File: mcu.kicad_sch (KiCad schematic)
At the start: 16 parts, among them J1 Conn_ARM_SWD_TagConnect_TC2030, U2 STM32L053R8Tx

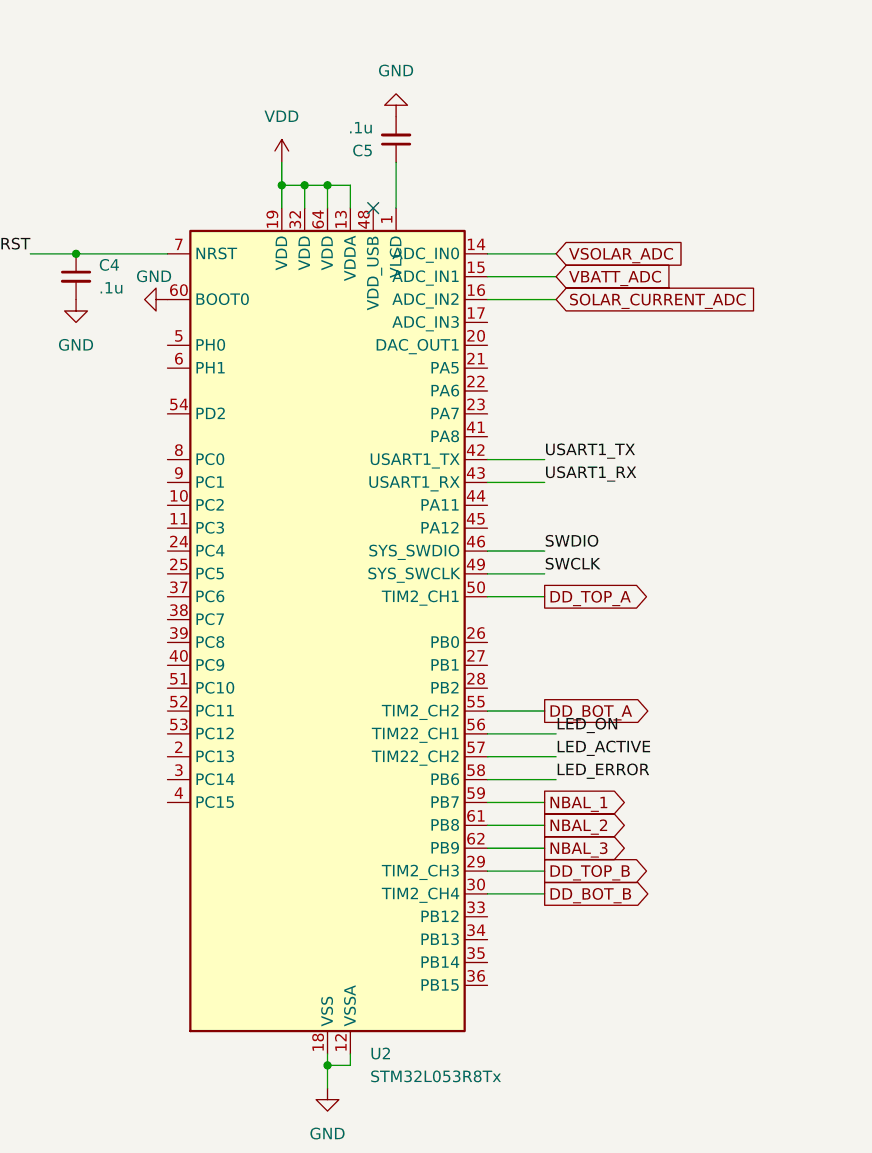
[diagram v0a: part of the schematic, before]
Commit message: Smaller diodes, more work
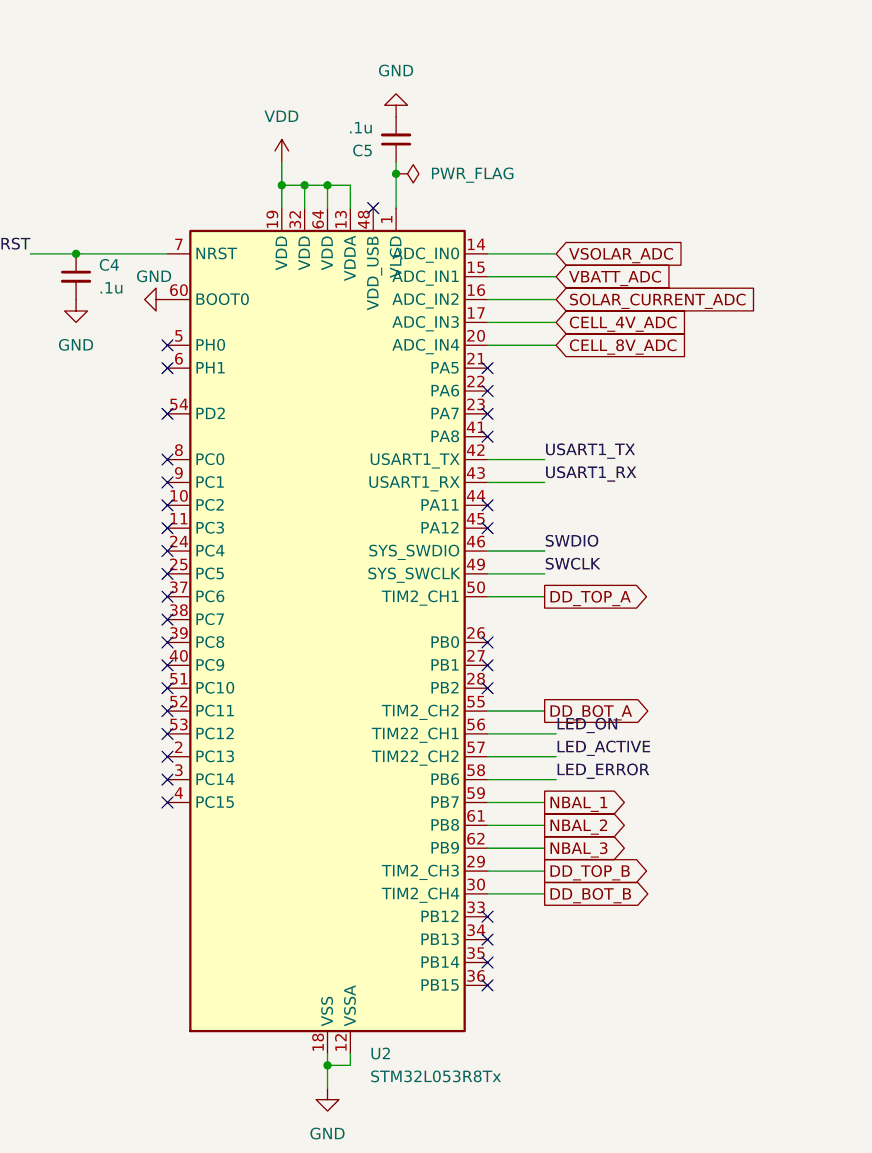
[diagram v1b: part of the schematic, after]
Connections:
- net CELL_4V_ADC: now reaches U2.17 (PA3)
- net CELL_8V_ADC: now reaches U2.20 (PA4)
- no-connect marks 3 -> 35
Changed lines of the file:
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@@
 		(color 0 0 0 0)
 	)
+	(junction
+		(at 148.59 41.91)
+		(diameter 0)
+		(color 0 0 0 0)
+	)
+	(no_connect
+		(at 123.19 99.06)
+	)
+	(no_connect
+		(at 123.19 88.9)
+	)
+	(no_connect
+		(at 158.75 132.08)
+	)
+	(no_connect
+		(at 158.75 63.5)
+	)
 	(no_connect
 		(at 64.77 62.23)
 	)
 	(no_connect
+		(at 158.75 78.74)
+	)
+	(no_connect
+		(at 158.75 96.52)
+	)
+	(no_connect
 		(at 68.58 41.91)
 	)
 	(no_connect
+		(at 158.75 99.06)
+	)
+	(no_connect
+		(at 158.75 81.28)
+	)
+	(no_connect
+		(at 123.19 96.52)
+	)
+	(no_connect
+		(at 123.19 91.44)
+	)
+	(no_connect
+		(at 158.75 71.12)
+	)
+	(no_connect
+		(at 158.75 68.58)
+	)
+	(no_connect
+		(at 123.19 73.66)
+	)
+	(no_connect
+		(at 123.19 93.98)
+	)
+	(no_connect
+		(at 123.19 76.2)
+	)
+	(no_connect
+		(at 123.19 81.28)
+	)
+	(no_connect
+		(at 123.19 106.68)
+	)
+	(no_connect
+		(at 123.19 111.76)
+	)
+	(no_connect
+		(at 123.19 101.6)
+	)
+	(no_connect
+		(at 123.19 83.82)
+	)
+	(no_connect
+		(at 123.19 68.58)
+	)
+	(no_connect
+		(at 158.75 127)
+	)
+	(no_connect
+		(at 158.75 124.46)
+	)
+	(no_connect
+		(at 123.19 86.36)
+	)
+	(no_connect
+		(at 158.75 93.98)
+	)
+	(no_connect
+		(at 123.19 104.14)
+	)
+	(no_connect
+		(at 123.19 63.5)
+	)
+	(no_connect
+		(at 123.19 78.74)
+	)
+	(no_connect
 		(at 146.05 45.72)
 	)
+	(no_connect
+		(at 158.75 129.54)
+	)
+	(no_connect
+		(at 158.75 66.04)
+	)
+	(no_connect
+		(at 123.19 60.96)
+	)
+	(no_connect
+		(at 123.19 109.22)
+	)
 	(wire
 		(pts
@@
 	(wire
 		(pts
-			(xy 148.59 40.64) (xy 148.59 45.72)
+			(xy 148.59 40.64) (xy 148.59 41.91)
 		)
 		(stroke
@@
 	(wire
 		(pts
+			(xy 148.59 41.91) (xy 148.59 45.72)
+		)
+		(stroke
+			(width 0)
+			(type default)
+		)
+	)
+	(wire
+		(pts
 			(xy 165.1 101.6) (xy 158.75 101.6)
 		)
@@
 	(wire
 		(pts
+			(xy 166.37 58.42) (xy 158.75 58.42)
+		)
+		(stroke
+			(width 0)
+			(type default)
+		)
+	)
+	(wire
+		(pts
 			(xy 68.58 36.83) (xy 73.66 36.83)
+		)
+		(stroke
+			(width 0)
+			(type default)
+		)
+	)
+	(wire
+		(pts
+			(xy 166.37 60.96) (xy 158.75 60.96)
 		)
 		(stroke
@@
 		)
 	)
+	(global_label "CELL_8V_ADC"
+		(shape input)
+		(at 166.37 60.96 0)
+		(fields_autoplaced yes)
+		(effects
+			(font
+				(size 1.27 1.27)
+			)
+			(justify left)
+		)
+		(property "Intersheetrefs" "${INTERSHEET_REFS}"
+			(at 181.6923 60.96 0)
+			(effects
+				(font
+					(size 1.27 1.27)
+				)
+				(justify left)
+				(hide yes)
+			)
+		)
+	)
 	(global_label "NBAL_2"
 		(shape output)
@@
 		(property "Intersheetrefs" "${INTERSHEET_REFS}"
 			(at 177.3985 119.38 0)
+			(effects
+				(font
+					(size 1.27 1.27)
+				)
+				(justify left)
+				(hide yes)
+			)
+		)
+	)
+	(global_label "CELL_4V_ADC"
+		(shape input)
+		(at 166.37 58.42 0)
+		(fields_autoplaced yes)
+		(effects
+			(font
+				(size 1.27 1.27)
+			)
+			(justify left)
+		)
+		(property "Intersheetrefs" "${INTERSHEET_REFS}"
+			(at 181.6923 58.42 0)
 			(effects
 				(font
@@
 		)
 		(pin "20"
-			(alternate "DAC_OUT1")
+			(alternate "ADC_IN4")
 		)
 		(pin "47"
@@
 					(unit 1)
 				)
+			)
+		)
+	)
+	(symbol
+		(lib_id "power:PWR_FLAG")
+		(at 148.59 41.91 270)
+		(unit 1)
+		(exclude_from_sim no)
+		(in_bom yes)
+		(on_board yes)
+		(dnp no)
+		(fields_autoplaced yes)
+		(property "Reference" "#FLG04"
+			(at 150.495 41.91 0)
+			(effects
+				(font
+					(size 1.27 1.27)
+				)
+				(hide yes)
+			)
+		)
+		(property "Value" "PWR_FLAG"
+			(at 152.4 41.9099 90)
+			(effects
+				(font
+					(size 1.27 1.27)
+				)
+				(justify left)
+			)
+		)
+		(property "Footprint" ""
+			(at 148.59 41.91 0)
+			(effects
+				(font
+					(size 1.27 1.27)
+				)
+				(hide yes)
+			)
+		)
+		(property "Datasheet" "~"
+			(at 148.59 41.91 0)
+			(effects
+				(font
+					(size 1.27 1.27)
+				)
+				(hide yes)
+			)
+		)
+		(property "Description" "Special symbol for telling ERC where power comes from"
+			(at 148.59 41.91 0)
+			(effects
+				(font
+					(size 1.27 1.27)
+				)
+				(hide yes)
+			)
+		)
+		(pin "1"
+		)
+		(instances
+			(project "JPBms2"
+				(path "/d86e471c-a8be-422d-a5d1-5a4699b7b766/852788cb-2266-4d4a-865c-a7e0873e4190"
+					(reference "#FLG04")
+					(unit 1)
+				)

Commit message: bom pt1
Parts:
- C6: footprint Capacitor_SMD:C_0805_2012Metric -> Capacitor_SMD:C_1206_3216Metric; LCSC_Code C15850 -> C13585
- UART1: LCSC_Code (none) -> C234195
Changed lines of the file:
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@@
+			)
+		)
+		(property "LCSC_Code" "C234195"
+			(at 59.69 64.77 0)
+			(effects
+				(font
+					(size 1.27 1.27)
+				)
+				(hide yes)
 			)
 		)
@@
 			)
 		)
-		(property "Footprint" "Capacitor_SMD:C_0805_2012Metric"
+		(property "Footprint" "Capacitor_SMD:C_1206_3216Metric"
 			(at 234.6452 34.29 0)
 			(effects
@@
 			)
 		)
-		(property "LCSC_Code" "C15850"
+		(property "LCSC_Code" "C13585"
 			(at 233.68 30.48 0)
 			(effects

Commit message: Assigning PNs
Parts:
- D1: LCSC_Code (none) -> C12624
- D2: LCSC_Code (none) -> C2287
- D3: LCSC_Code (none) -> C2286
- R1, R2, R3: LCSC_Code (none) -> C22808
- U2: LCSC_Code (none) -> C784738
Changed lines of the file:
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@@
+			)
+		)
+		(property "LCSC_Code" "C2286"
+			(at 254 86.36 0)
+			(effects
+				(font
+					(size 1.27 1.27)
+				)
+				(hide yes)
 			)
 		)
@@
 			)
 		)
+		(property "LCSC_Code" "C784738"
+			(at 140.97 93.98 0)
+			(effects
+				(font
+					(size 1.27 1.27)
+				)
+				(hide yes)
+			)
+		)
 		(pin "22"
 		)
@@
 			)
 		)
+		(property "LCSC_Code" "C12624"
+			(at 254 68.58 0)
+			(effects
+				(font
+					(size 1.27 1.27)
+				)
+				(hide yes)
+			)
+		)
 		(pin "1"
 		)
@@
 			)
 		)
+		(property "LCSC_Code" "C2287"
+			(at 254 77.47 0)
+			(effects
+				(font
+					(size 1.27 1.27)
+				)
+				(hide yes)
+			)
+		)
 		(pin "1"
 		)
@@
 			)
 		)
+		(property "LCSC_Code" "C22808"
+			(at 240.03 86.36 0)
+			(effects
+				(font
+					(size 1.27 1.27)
+				)
+				(hide yes)
+			)
+		)
 		(pin "1"
 		)
@@
 			)
 		)
+		(property "LCSC_Code" "C22808"
+			(at 240.03 68.58 0)
+			(effects
+				(font
+					(size 1.27 1.27)
+				)
+				(hide yes)
+			)
+		)
 		(pin "1"
 		)
@@
 			(at 240.03 77.47 0)
 			(effects
+				(font
+					(size 1.27 1.27)
+				)
+				(hide yes)
+			)
+		)
+		(property "LCSC_Code" "C22808"
+			(at 240.03 77.47 0)
+			(effects

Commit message: sent to jlcpcb
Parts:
- D1: value LED -> LED_G
- D2: value LED -> LED_Y
- D3: value LED -> LED_R
- UART1: value Conn_01x04 -> Conn_01x04 Picoblade
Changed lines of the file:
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@@
 			)
 		)
-		(property "Value" "LED"
+		(property "Value" "LED_R"
 			(at 252.4125 82.55 0)
 			(effects
@@
 			)
 		)
-		(property "Value" "Conn_01x04"
+		(property "Value" "Conn_01x04 Picoblade"
 			(at 57.15 67.3099 0)
 			(effects
@@
 			)
 		)
-		(property "Value" "LED"
+		(property "Value" "LED_G"
 			(at 252.4125 64.77 0)
 			(effects
@@
 			)
 		)
-		(property "Value" "LED"
+		(property "Value" "LED_Y"
 			(at 252.4125 73.66 0)
 			(effects

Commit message: New design and layout
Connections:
- net GND: now also D1.1 (K), D2.1 (K), D3.1 (K)
- net VBATT_ADC: now also U2.14 (PA0); no longer U2.15 (PA1)
- net VDD: no longer D1.2 (A), D2.2 (A), D3.2 (A)
- net VSOLAR_ADC: now also U2.15 (PA1); no longer U2.14 (PA0)
- net at R3.2: now also D3.2 (A); no longer D3.1 (K)
- net at R1.2: now also D1.2 (A); no longer D1.1 (K)
- net at R2.2: now also D2.2 (A); no longer D2.1 (K)
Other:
- moved on the sheet: D1, D2, D3
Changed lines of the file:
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@@
+	)
+	(junction
+		(at 264.16 86.36)
+		(diameter 0)
+		(color 0 0 0 0)
 	)
 	(junction
@@
 	)
 	(junction
-		(at 264.16 68.58)
-		(diameter 0)
-		(color 0 0 0 0)
-	)
-	(junction
 		(at 250.19 26.67)
 		(diameter 0)
@@
 	(wire
 		(pts
+			(xy 264.16 88.9) (xy 264.16 86.36)
+		)
+		(stroke
+			(width 0)
+			(type default)
+		)
+	)
+	(wire
+		(pts
 			(xy 158.75 111.76) (xy 165.1 111.76)
 		)
@@
 		(pts
 			(xy 140.97 45.72) (xy 140.97 43.18)
-		)
-		(stroke
-			(width 0)
-			(type default)
-		)
-	)
-	(wire
-		(pts
-			(xy 264.16 63.5) (xy 264.16 68.58)
 		)
 		(stroke
@@
 	(global_label "VBATT_ADC"
 		(shape input)
-		(at 166.37 53.34 0)
+		(at 166.37 50.8 0)
 		(fields_autoplaced yes)
 		(effects
@@
 		)
 		(property "Intersheetrefs" "${INTERSHEET_REFS}"
-			(at 179.3338 53.34 0)
+			(at 179.3338 50.8 0)
 			(effects
 				(font
@@
 	(global_label "VSOLAR_ADC"
 		(shape input)
-		(at 166.37 50.8 0)
+		(at 166.37 53.34 0)
 		(fields_autoplaced yes)
 		(effects
@@
 		)
 		(property "Intersheetrefs" "${INTERSHEET_REFS}"
-			(at 180.9667 50.8 0)
+			(at 180.9667 53.34 0)
 			(effects
 				(font
@@
 	(symbol
 		(lib_id "Device:LED")
-		(at 254 86.36 0)
+		(at 254 86.36 180)
 		(unit 1)
 		(exclude_from_sim no)
@@
 		(fields_autoplaced yes)
 		(property "Reference" "D3"
-			(at 252.4125 80.01 0)
+			(at 255.5875 78.74 0)
 			(effects
 				(font
@@
 		)
 		(property "Value" "LED_R"
-			(at 252.4125 82.55 0)
+			(at 255.5875 81.28 0)
 			(effects
 				(font
@@
 	(symbol
 		(lib_id "Device:LED")
-		(at 254 68.58 0)
+		(at 254 68.58 180)
 		(unit 1)
 		(exclude_from_sim no)
@@
 		(fields_autoplaced yes)
 		(property "Reference" "D1"
-			(at 252.4125 62.23 0)
+			(at 255.5875 60.96 0)
 			(effects
 				(font
@@
 		)
 		(property "Value" "LED_G"
-			(at 252.4125 64.77 0)
+			(at 255.5875 63.5 0)
 			(effects
 				(font
@@
 	)
 	(symbol
+		(lib_id "power:GND")
+		(at 264.16 88.9 0)
+		(unit 1)
+		(exclude_from_sim no)
+		(in_bom yes)
+		(on_board yes)
+		(dnp no)
+		(fields_autoplaced yes)
+		(property "Reference" "#PWR015"
+			(at 264.16 95.25 0)
+			(effects
+				(font
+					(size 1.27 1.27)
+				)
+				(hide yes)
+			)
+		)
+		(property "Value" "GND"
+			(at 264.16 93.98 0)
+			(effects
+				(font
+					(size 1.27 1.27)
+				)
+			)
+		)
+		(property "Footprint" ""
+			(at 264.16 88.9 0)
+			(effects
+				(font
+					(size 1.27 1.27)
+				)
+				(hide yes)
+			)
+		)
+		(property "Datasheet" ""
+			(at 264.16 88.9 0)
+			(effects
+				(font
+					(size 1.27 1.27)
+				)
+				(hide yes)
+			)
+		)
+		(property "Description" "Power symbol creates a global label with name \"GND\" , ground"
+			(at 264.16 88.9 0)
+			(effects
+				(font
+					(size 1.27 1.27)
+				)
+				(hide yes)
+			)
+		)
+		(pin "1"
+		)
+		(instances
+			(project "JPBms2"
+				(path "/d86e471c-a8be-422d-a5d1-5a4699b7b766/852788cb-2266-4d4a-865c-a7e0873e4190"
+					(reference "#PWR015")
+					(unit 1)
+				)
+			)
+		)
+	)
+	(symbol
 		(lib_id "Device:C_Small")
 		(at 148.59 38.1 180)
@@
 	)
 	(symbol
-		(lib_id "power:VDD")
-		(at 264.16 63.5 0)
+		(lib_id "Device:LED")
+		(at 254 77.47 180)
 		(unit 1)
 		(exclude_from_sim no)
@@
 		(on_board yes)
 		(dnp no)
-		(property "Reference" "#PWR015"
-			(at 264.16 67.31 0)
-			(effects
-				(font
-					(size 1.27 1.27)
-				)
-				(hide yes)
-			)
-		)
-		(property "Value" "VDD"
-			(at 264.16 58.42 0)
-			(effects
-				(font
-					(size 1.27 1.27)
-				)
-			)
-		)
-		(property "Footprint" ""
-			(at 264.16 63.5 0)
-			(effects
-				(font
-					(size 1.27 1.27)
-				)
-				(hide yes)
-			)
-		)
-		(property "Datasheet" ""
-			(at 264.16 63.5 0)
-			(effects
-				(font
-					(size 1.27 1.27)
-				)
-				(hide yes)
-			)
-		)
-		(property "Description" "Power symbol creates a global label with name \"VDD\""
-			(at 264.16 63.5 0)
-			(effects
-				(font
-					(size 1.27 1.27)
-				)
-				(hide yes)
-			)
-		)
-		(pin "1"
-		)
-		(instances
-			(project "JPBms2"
-				(path "/d86e471c-a8be-422d-a5d1-5a4699b7b766/852788cb-2266-4d4a-865c-a7e0873e4190"
-					(reference "#PWR015")
-					(unit 1)
-				)
-			)
-		)
-	)
-	(symbol
-		(lib_id "Device:LED")
-		(at 254 77.47 0)
-		(unit 1)
-		(exclude_from_sim no)
-		(in_bom yes)
-		(on_board yes)
-		(dnp no)
 		(fields_autoplaced yes)
 		(property "Reference" "D2"
-			(at 252.4125 71.12 0)
+			(at 255.5875 69.85 0)
 			(effects
 				(font
@@
 		)
 		(property "Value" "LED_Y"
-			(at 252.4125 73.66 0)
-			(effects
-				(font
+			(at 255.5875 72.39 0)
+			(effects
+				(font
